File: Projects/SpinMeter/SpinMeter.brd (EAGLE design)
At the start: 85 x 30 mm, 30 parts, among them IC1 LIS2DW12TR, Q1 2N7002, Q2 2N7002, Q3 BSS84LT1G, U1 BMG250, U2 FDC1004DSCT, U3 BAT-HLD-001-THM

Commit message: Finished board
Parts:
- removed Q3: BSS84LT1G, MOSFETS:SOT23-3
- added D1: BAT54H, Diodes:SOD123F
- added R8: (no value), rcl:R0201
- added R9: 100k, rcl:R0603
- added T2: BSS84, nxp_60:SOT23
- added U$10: SKRMAAE010, Buttons:SKRMAAE010
- added U$3: IDC_SHIELD, IDC:SHIELD_IDC
- added U$4: 36003250S, Shields:36003250S
- added U$5, U$6, U$7, U$8: TESTPOINT_22, test_points:TESTPOINT_22
- added U$9: TPS7A0531PDBVR, PowerSupplies:SOT753
- R1, R2, R3, R4: value (none) -> 22k
- moved R5 21.5 mm to (63.6, 4.19)
- moved C9 11.7 mm to (71.1, 8.37), turned to 0 degrees
- moved C10 7.75 mm to (68.4, 8.06), turned to 270 degrees
- moved C1 6.76 mm to (22.0, 3.30), turned to 90 degrees
- moved U3 4.59 mm to (14.0, 15.0)
- moved R2 3.88 mm to (67.0, 4.16), turned to 270 degrees
- moved IC1 3.85 mm to (65.7, 7.48), turned to 0 degrees
- moved LED1 2.33 mm to (58.6, 25.1), turned to 270 degrees
- moved U$2 2.00 mm to (28.0, 15.0)
- moved Q1 1.55 mm to (62.7, 9.05)
- moved U2 0.99 mm to (56.5, 15.0)
- moved R1 0.90 mm to (59.9, 7.84)
- moved R4 0.76 mm to (66.8, 13.8)
- moved Y1 0.68 mm to (71.4, 22.1)
- moved R6 0.46 mm to (58.6, 26.8), turned to 0 degrees
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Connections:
- new net BTN: U$10.P$1, U$10.P$3, U4.P6
- new net HV_EN: U$9.3, U4.P38
- new net N$10: R8.1, U2.1
- new net N$9: R5.1, R9.1, T2.1
- new net SHIELD: R8.2, U$3.P$1, U$4.P$1, U$4.P$2, U$4.P$3, U$4.P$4
- new net VDD: C1.1, D1.2, U$9.1, U3.1, U3.2, U3.3, U3.4
- net !VCCINT_EN: now also R9.2, U4.P37; no longer Q3.G, R5.2, U4.P19
- net 0V: now also U$10.P$2, U$10.P$4, U$5.P$1, U$9.2
- net SCL_LV: now also U$7.P$1
- net SDA_LV: now also U$6.P$1
- net VCC: now also D1.1, R5.2, T2.2, U$9.5; no longer C1.1, Q3.S, R5.1, U3.1, U3.2, U3.3, U3.4
- net VCCINT: now also T2.3, U$8.P$1; no longer Q3.D
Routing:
- net 0V: track 7.21 -> 114.1 mm, vias 0 -> 47
- net VDD: track 0.00 -> 67.1 mm, vias 0 -> 2
- net VCC: track 0.00 -> 58.8 mm, vias 0 -> 2
- net VCCINT: track 14.3 -> 56.6 mm, vias 0 -> 2
- net HV_EN: track 0.00 -> 22.7 mm, vias 0 -> 2
- net BTN: track 0.00 -> 20.8 mm
- net SHIELD: track 0.00 -> 15.3 mm, vias 0 -> 8
- net N$10: track 0.00 -> 9.09 mm
- net SDA: track 8.64 -> 17.7 mm, vias 0 -> 2
- net SCL: track 5.74 -> 13.1 mm, vias 0 -> 3
- net LIS_INT2: track 16.1 -> 9.42 mm, vias 0 -> 2
- net LIS_INT1: track 14.1 -> 8.49 mm, vias 0 -> 2
- net N$9: track 0.00 -> 3.37 mm
- net N$1: track 12.5 -> 11.4 mm
- net N$2: track 12.6 -> 11.6 mm
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- added copper zone on layer 1, net 0V
- added copper zone on layer 16, net 0V
- added copper zone on layer 16, net SHIELD
- added copper zone on layer 1, net VCCINT
- added copper zone on layer 1, net VDD

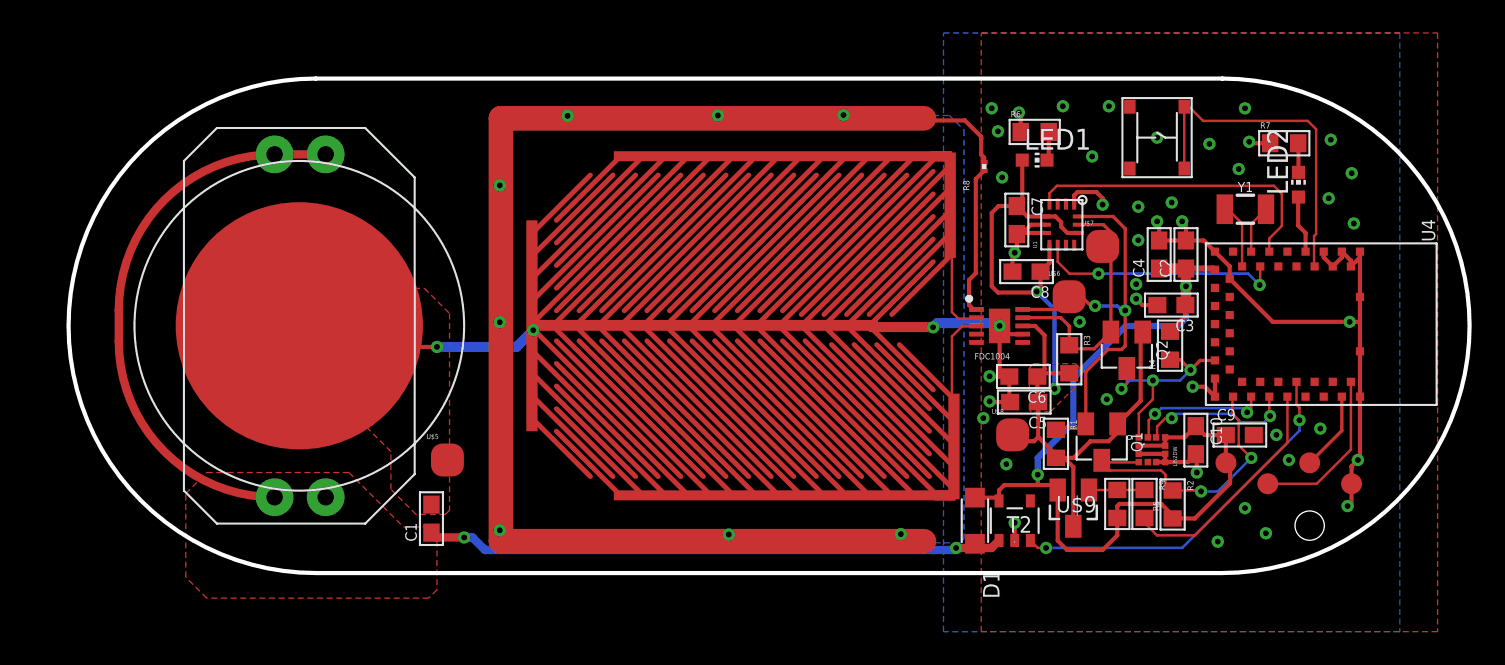
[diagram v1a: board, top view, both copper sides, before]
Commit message: Massive library update Added projects Added 3D packages
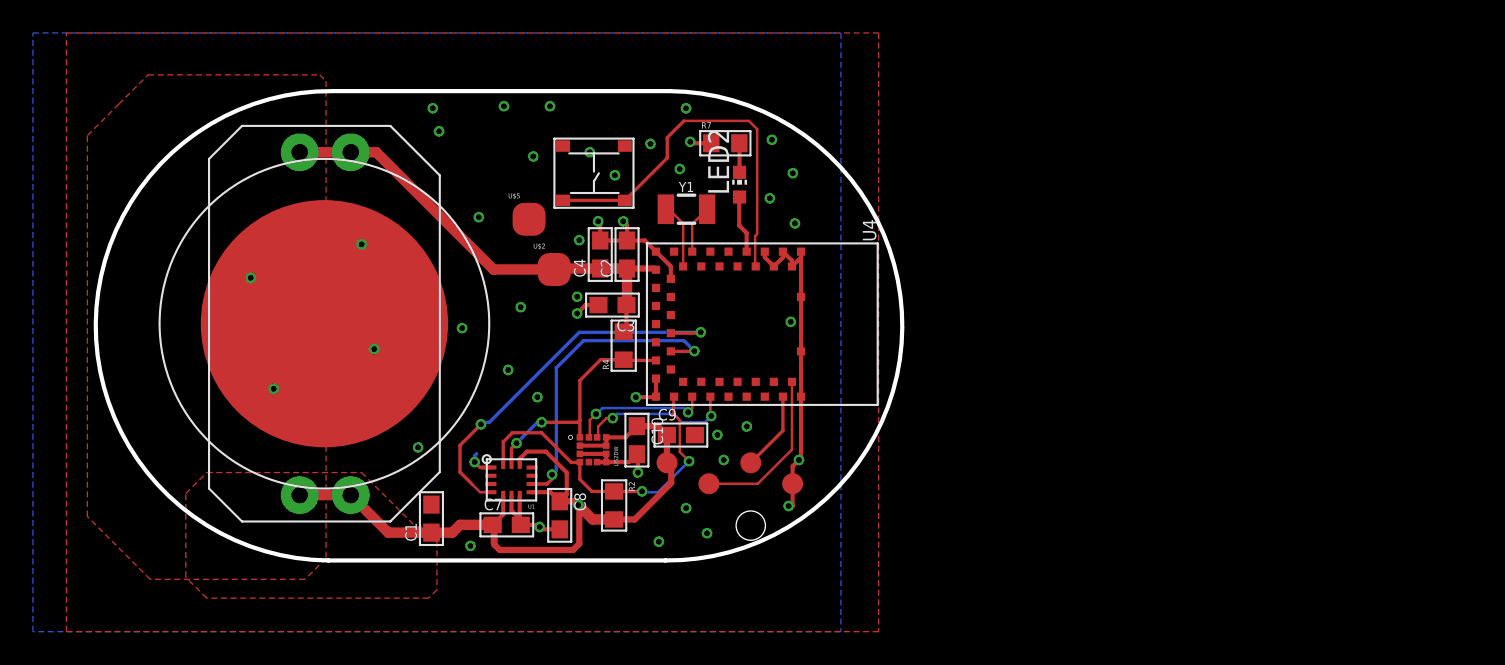
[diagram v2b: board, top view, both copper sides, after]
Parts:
- removed C5: 100nF, rcl:C0603
- removed C6: 10uF, rcl:C0603
- removed D1: BAT54H, Diodes:SOD123F
- removed LED1: (no value), adafruit:CHIP-LED0603
- removed Q1, Q2: 2N7002, MOSFETS:SOT23-3
- removed R1, R3: 22k, rcl:R0603
- removed R5, R9: 100k, rcl:R0603
- removed R6: 330, rcl:R0603
- removed R8: (no value), rcl:R0201
- removed T2: BSS84, nxp_60:SOT23
- removed U$3: IDC_SHIELD, IDC:SHIELD_IDC
- removed U$4: 36003250S, Shields:36003250S
- removed U$6, U$7, U$8: TESTPOINT_22, test_points:TESTPOINT_22
- removed U$9: TPS7A0531PDBVR, PowerSupplies:SOT753
- removed U2: FDC1004DSCT, ADC:SON50P300X300X80-11N
- U$2: value IDC_SHEAR -> TESTPOINT_22; device IDC:SHEAR_12/6 -> test_points:TESTPOINT_22
- moved U1 36.8 mm to (26.9, 5.65), turned to 0 degrees
- moved C7 36.1 mm to (26.6, 2.92), turned to 0 degrees
- moved U$10 34.2 mm to (31.9, 24.3), turned to 180 degrees
- moved C2 33.9 mm to (33.9, 19.3)
- moved C3 33.9 mm to (33.0, 16.3)
- moved IC1 33.9 mm to (31.8, 7.48)
- moved U$1 33.9 mm to (40.1, 5.42)
- moved C10 33.9 mm to (34.5, 8.06)
- moved C4 33.9 mm to (32.3, 19.3)
- moved LED2 33.9 mm to (40.7, 23.6)
- moved U4 33.9 mm to (35.1, 20.0)
- moved Y1 33.9 mm to (37.5, 22.1)
- moved C9 33.9 mm to (37.2, 8.37)
- moved R7 33.9 mm to (39.8, 26.1)
- moved R2 33.9 mm to (33.1, 4.10)
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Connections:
- removed net !VCCINT_EN: R9.2, U4.P37
- removed net HV_EN: U$9.3, U4.P38
- removed net N$1: U$2.P$2, U2.2
- removed net N$10: R8.1, U2.1
- removed net N$2: U$2.P$3, U2.3
- removed net N$5: LED1.C, R6.2
- removed net N$9: R5.1, R9.1, T2.1
- removed net SCL_LV: Q2.S, R3.1, U$7.P$1, U1.P$13, U2.9
- removed net SDA_LV: Q1.S, R1.1, U$6.P$1, U1.P$14, U2.10
- removed net SHIELD: R8.2, U$3.P$1, U$4.P$1, U$4.P$2, U$4.P$3, U$4.P$4
- removed net VCCINT: C5.1, C6.1, C7.1, C8.1, LED1.A, Q1.G, Q2.G, R1.2, R3.2, T2.3, U$8.P$1, U1.P$12, U1.P$5, U1.P$8, U2.8
- removed net VDD: C1.1, D1.2, U$9.1, U3.1, U3.2, U3.3, U3.4
- net 0V: no longer C5.2, C6.2, R6.1, U$2.P$1, U$9.2, U2.11, U2.7
- net GYR_INT1: now also U4.P24; no longer U4.P11
- net GYR_INT2: now also U4.P26; no longer U4.P12
- net SCL: now also U1.P$13; no longer Q2.D
- net SDA: now also U1.P$14; no longer Q1.D
- net VCC: now also C1.1, C7.1, C8.1, U$2.P$1, U1.P$12, U1.P$5, U1.P$8, U3.1, U3.2, U3.3, U3.4; no longer D1.1, R5.2, T2.2, U$9.5
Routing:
- net VDD: track 67.1 -> 0.00 mm, vias 2 -> 0
- net 0V: track 114.1 -> 48.3 mm, vias 47 -> 44
- net VCCINT: track 56.6 -> 0.00 mm, vias 2 -> 0
- net SDA_LV: track 26.1 -> 0.00 mm, vias 2 -> 0
- net HV_EN: track 22.7 -> 0.00 mm, vias 2 -> 0
- net VCC: track 58.8 -> 80.6 mm, vias 2 -> 1
- net SCL_LV: track 16.4 -> 0.00 mm
- net SHIELD: track 15.3 -> 0.00 mm, vias 8 -> 0
- net !VCCINT_EN: track 14.4 -> 0.00 mm
- net N$2: track 11.6 -> 0.00 mm
- net N$1: track 11.4 -> 0.00 mm
- net N$10: track 9.09 -> 0.00 mm
- net GYR_INT1: track 19.0 -> 23.3 mm, vias 0 -> 2
- net GYR_INT2: track 15.0 -> 18.9 mm
- net N$9: track 3.37 -> 0.00 mm
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- added copper zone on layer 1, net VCC
- removed copper zone on layer 16, net SHIELD
- removed copper zone on layer 1, net VCCINT
- removed copper zone on layer 1, net VDD
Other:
- board size 85 x 30 mm -> 48.9 x 28.5 mm
